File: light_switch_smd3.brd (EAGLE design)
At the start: 36.6 x 44.7 mm, 17 parts, among them J2 SW1, T1 BT136, U1 LM1117

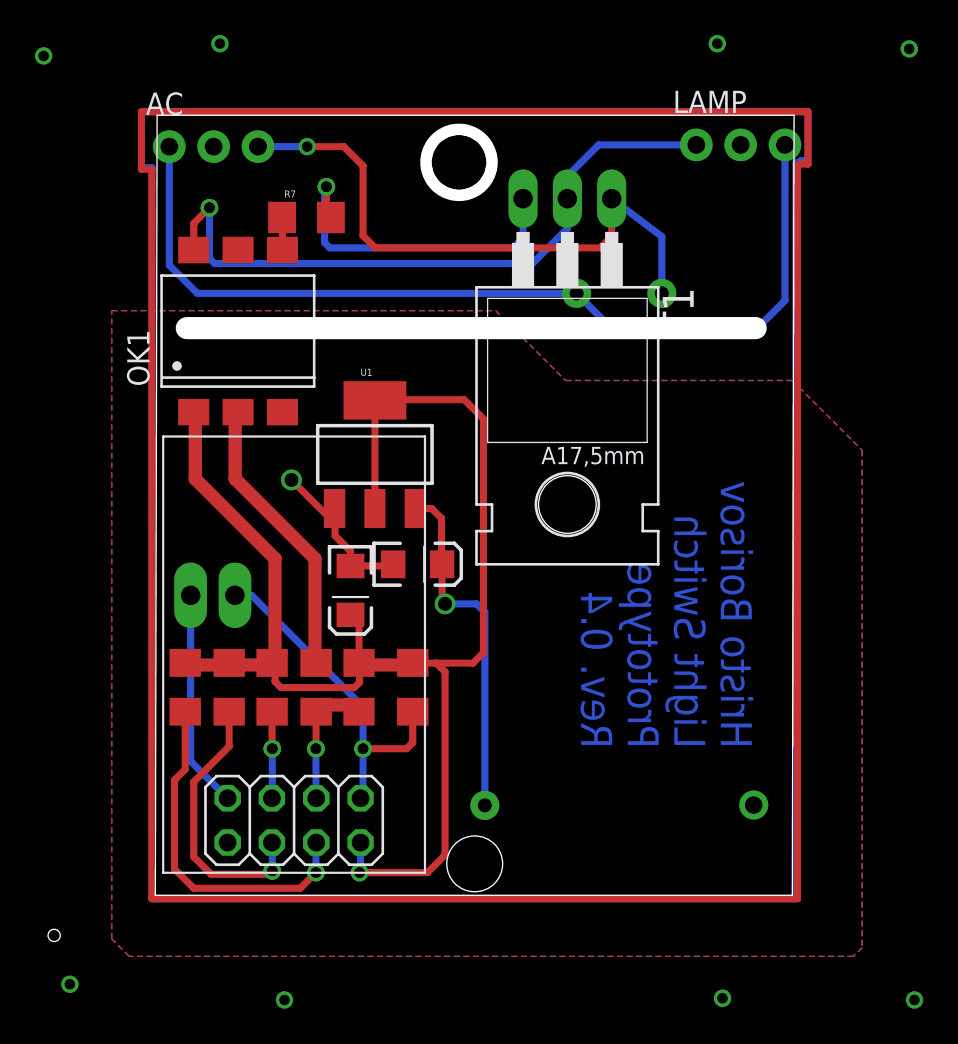
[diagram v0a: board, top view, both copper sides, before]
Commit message: Version 5 ready and works. Minor correction on the triac placement
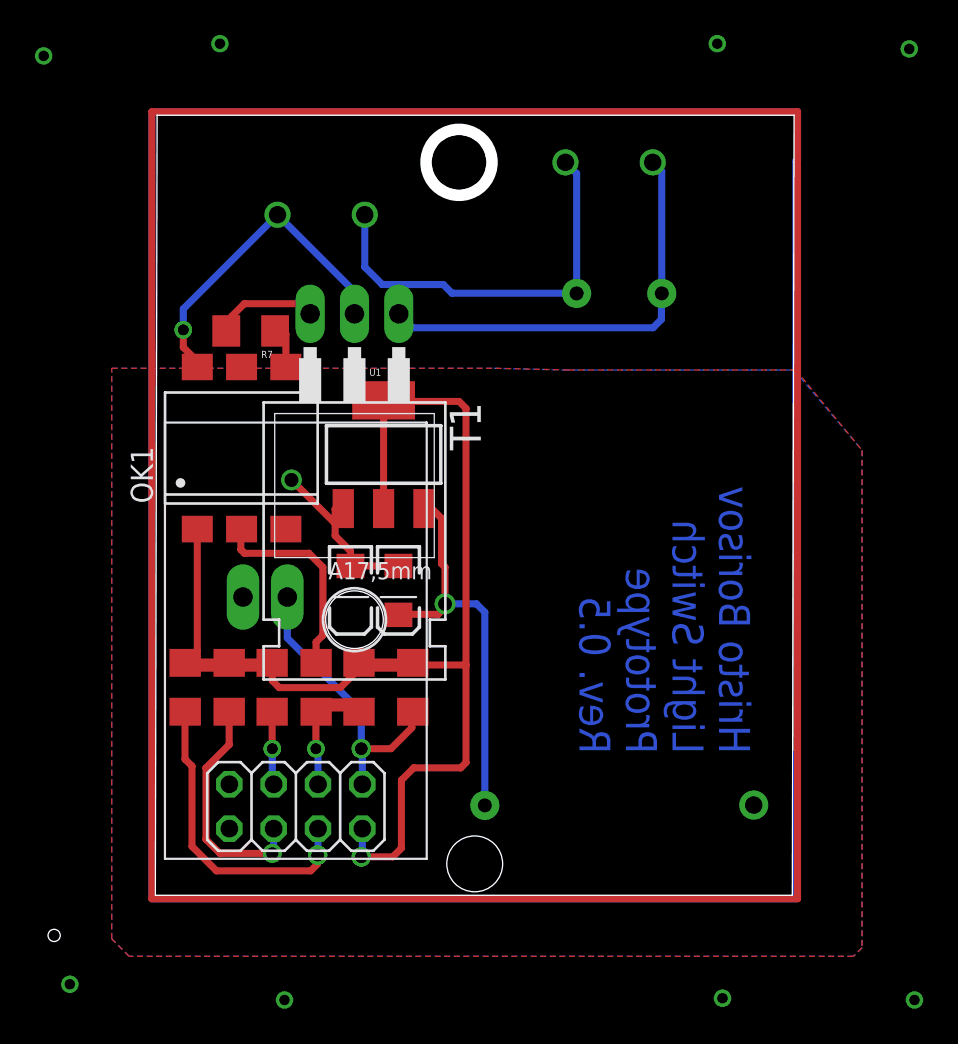
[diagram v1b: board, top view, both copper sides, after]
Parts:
- AC: value AC -> DG306-5.0; device SparkFun-Connectors:1X03_NO_SILK -> myblog_library:DG306-PCKG
- LAMP: value LAMP -> DG306-5.0; device SparkFun-Connectors:1X03_NO_SILK -> myblog_library:DG306-PCKG
- moved AC 25.2 mm to (26.0, 41.0)
- moved LAMP 21.9 mm to (9.50, 38.0)
- moved T1 13.9 mm to (11.4, 26.0)
- moved R7 7.24 mm to (5.46, 31.3), turned to 180 degrees
- moved OK1 6.70 mm to (4.94, 24.6)
- moved J2 3.00 mm to (5.02, 16.1)
- moved C2 1.86 mm to (13.9, 16.5), turned to 270 degrees
- moved U$2 0.81 mm to (10.1, 4.09)
- moved U1 0.50 mm to (13.1, 24.3)
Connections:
- net N$11: now also AC.P$1, LAMP.P$2; no longer AC.1, LAMP.3
- net N$12: now also AC.P$2; no longer AC.3
- net N$8: now also LAMP.P$1; no longer LAMP.1
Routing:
- net N$11: track 52.9 -> 23.5 mm
- net N$8: track 38.3 -> 18.8 mm
- net N$6: track 19.1 -> 6.00 mm, vias 1 -> 0
- net GND: track 22.2 -> 10.4 mm, vias 0 -> 1
- net N$3: track 84.2 -> 72.6 mm
- net N$12: track 34.3 -> 24.8 mm, vias 1 -> 0
- net N$5: track 16.4 -> 12.0 mm
- net N$1: track 20.0 -> 16.8 mm
- net N$13: track 20.3 -> 22.8 mm
- net N$2: track 15.8 -> 13.5 mm
- net N$32: track 166.4 -> 164.1 mm
- net N$31: track 166.3 -> 164.1 mm
- net N$4: track 19.9 -> 17.9 mm
- net N$14: track 4.97 -> 4.20 mm
- net N$9: track 7.75 -> 6.99 mm
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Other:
- outline, holes or cut-outs redrawn
- board text added: "Hristo Borisov Light Switch Prototype Rev. 0.5"
- board text removed: "Hristo Borisov Light Switch Prototype Rev. 0.4"

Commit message: Addign milling information
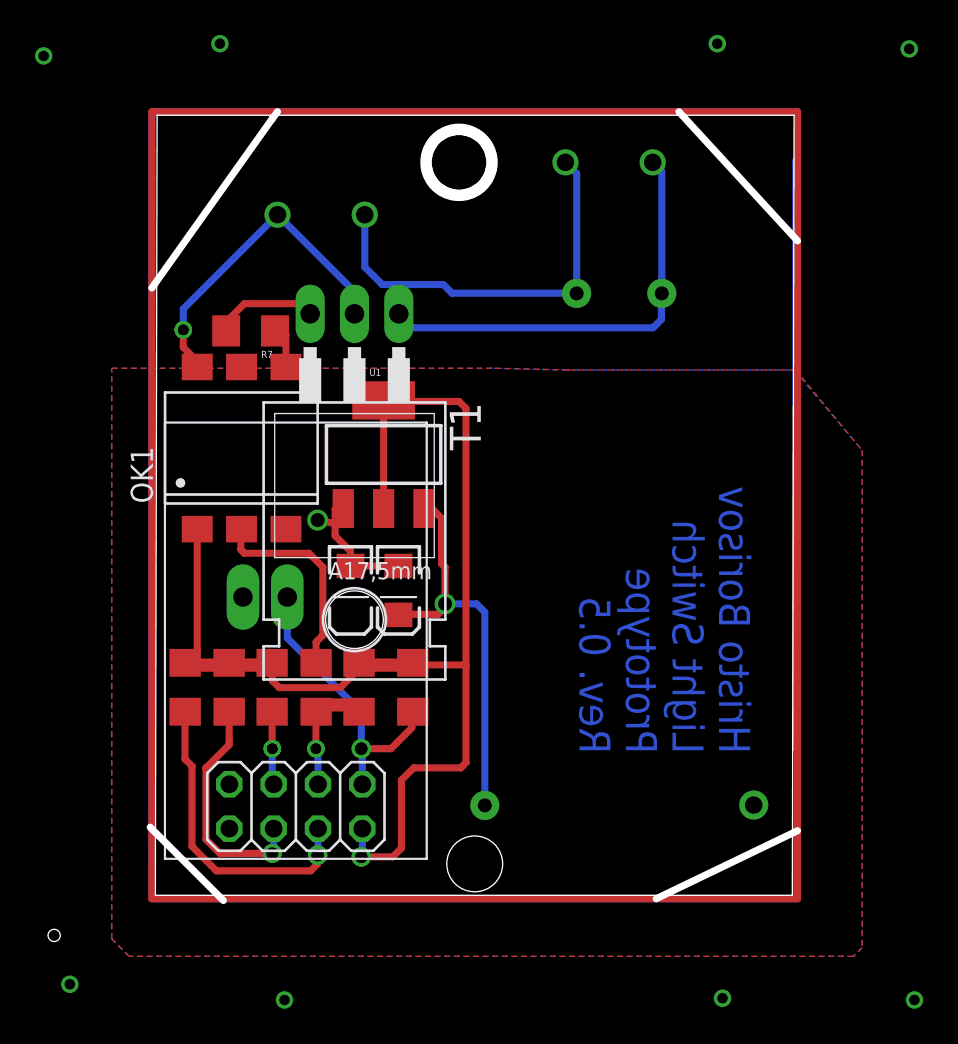
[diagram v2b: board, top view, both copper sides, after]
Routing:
- net GND: track 10.4 -> 7.86 mm
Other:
- board size 36.6 x 44.7 mm -> 37.1 x 45.2 mm
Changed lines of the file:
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@@
 Prototype
 Rev. 0.5</text>
+<wire x1="6.7" y1="43.5" x2="-0.2" y2="33.8" width="0.4064" layer="46"/>
+<wire x1="6.7" y1="43.5" x2="7" y2="43.9" width="0.4064" layer="46"/>
+<wire x1="30" y1="43.9" x2="36.8" y2="36.5" width="0.4064" layer="46"/>
+<wire x1="36.8" y1="2.7" x2="28.7" y2="-1.2" width="0.4064" layer="46"/>
+<wire x1="3.9" y1="-1.3" x2="-0.3" y2="2.9" width="0.4064" layer="46"/>
 </plain>
 <attributes>
@@
 <wire x1="10.3" y1="21.1298" x2="10.7686" y2="21.1612" width="0.4064" layer="1"/>
 <wire x1="10.3" y1="19.6" x2="10.3" y2="20.3" width="0.4064" layer="1"/>
-<wire x1="10.3" y1="20.3" x2="7.8" y2="22.8" width="0.4064" layer="1"/>
-<via x="7.8" y="22.8" extent="1-16" drill="0.8"/>
+<wire x1="10.3" y1="20.3" x2="9.3" y2="20.5" width="0.4064" layer="1"/>
+<via x="9.3" y="20.5" extent="1-16" drill="0.8"/>
 </signal>
 <signal name="N$3">
